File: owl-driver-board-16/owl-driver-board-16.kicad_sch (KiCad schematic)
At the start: 80 parts, among them J10 1890963, J11 ENABLE, J2 RASPBERRYPI-40-PIN-GPIO, J25 CONN_04X2, J27 CONN_04X2, J29 CONN_04X2, J6 CONN_04X2, J9 PI 5V, U1 TPS54531DDA, U3 LM73100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

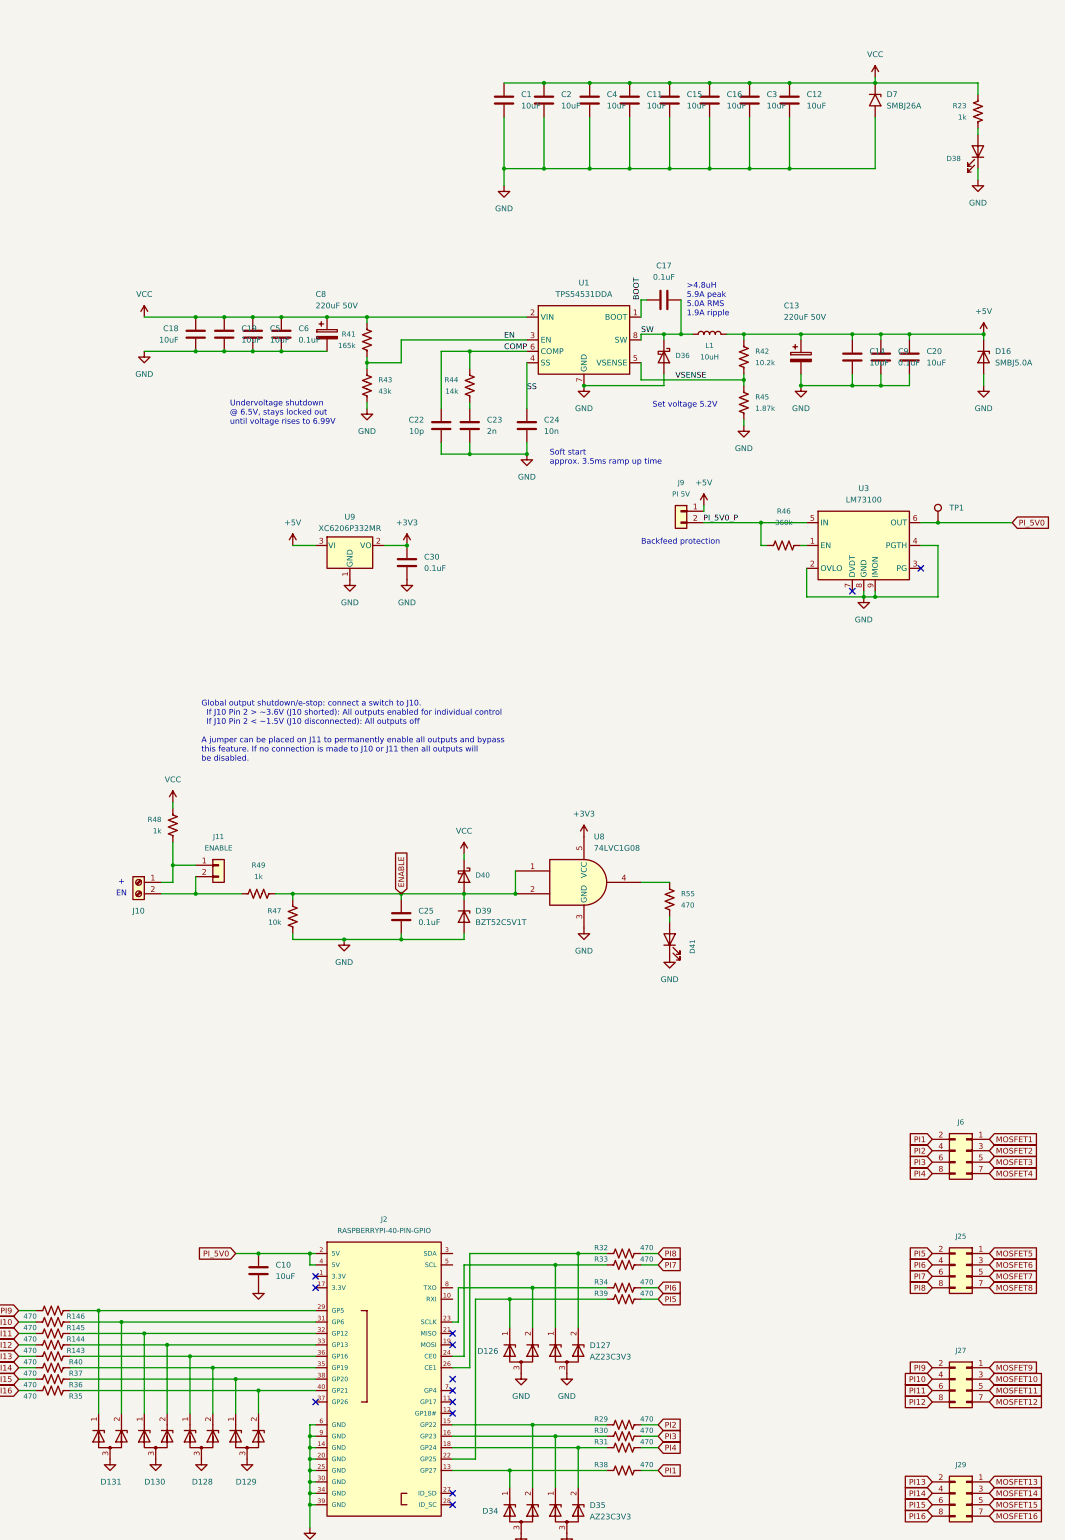
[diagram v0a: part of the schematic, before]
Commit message: add a 16-way version
Add a 16-way version of the HAT. Drop the PWM controller to focus on
GPIO control of 16 outputs, with output enable/e-stop, and keeping the
25W Pi power supply.

This version (v1.0) has a small bug in the panel, fixed in v1.1.
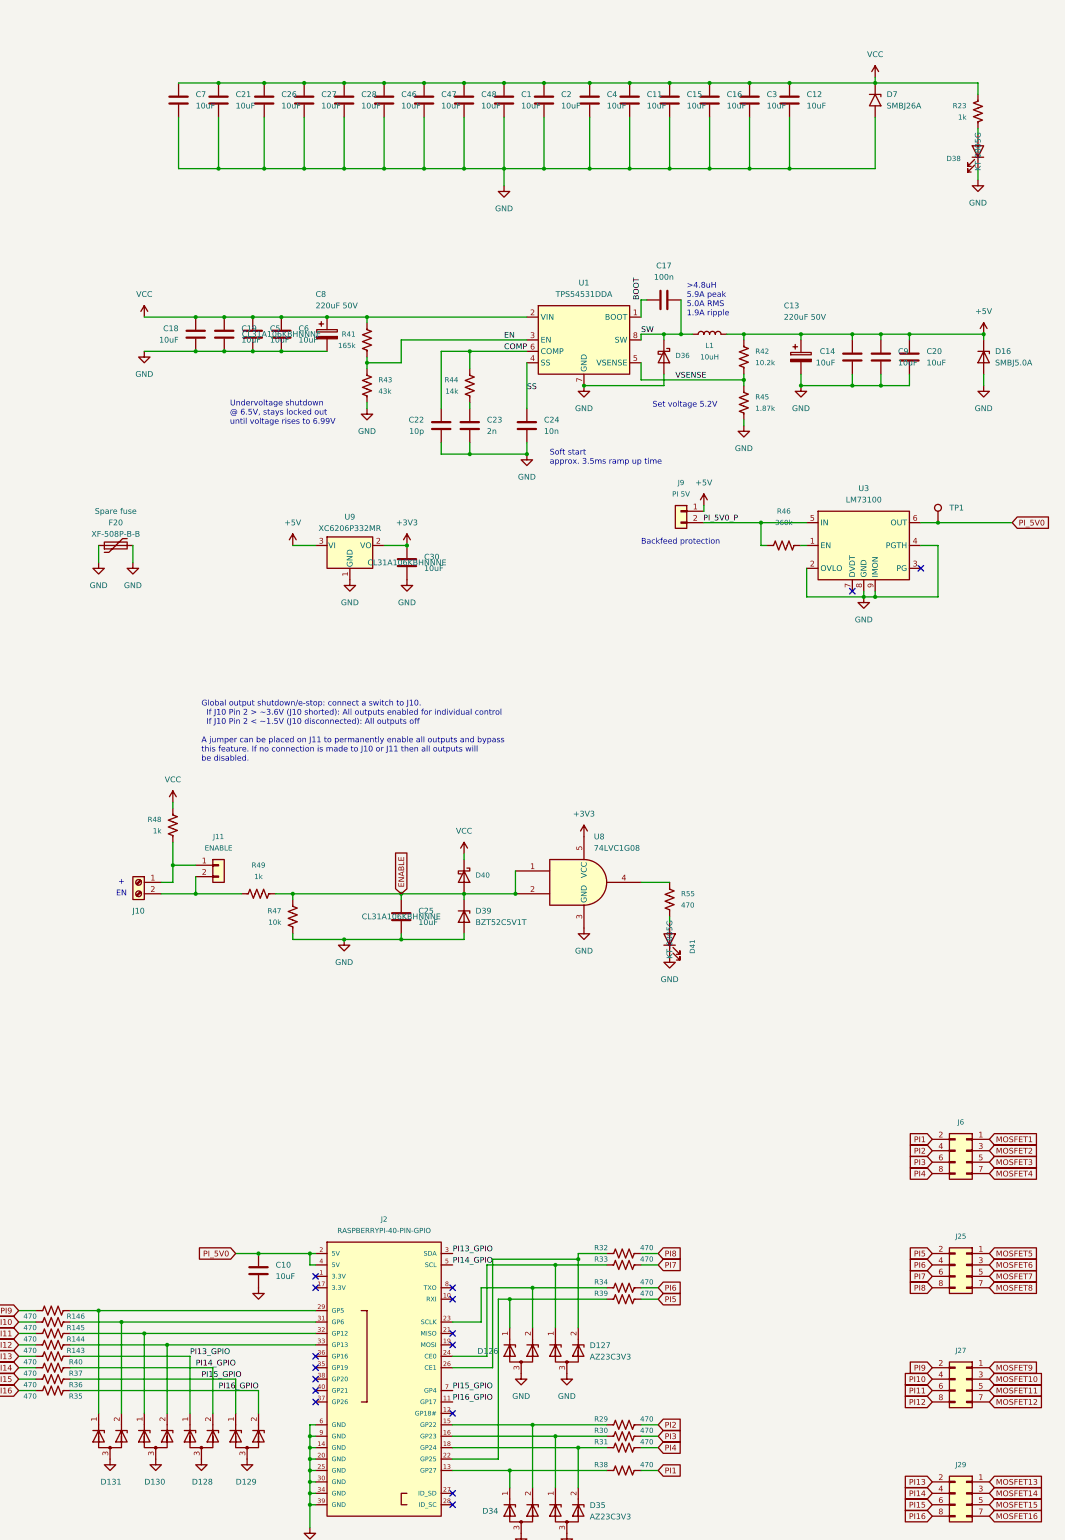
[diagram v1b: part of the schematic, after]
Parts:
- added C21, C26, C27, C28, C46, C47, C48, C7: 10uF, misc:C_1206_3216Metric_nosilk, symbol Device:C
- added F20: XF-508P-B-B, Fuse:Fuseholder_Blade_Mini_Keystone_3568, symbol Device:Polyfuse
- C1, C10, C11, C12, C14, C15, C16, C18, C19, C2, C20, C3, C4, C5: LCSC C89835 -> C13585; Part 1206X106K500CT -> CL31A106KBHNNNE
- C17: value 0.1uF -> 100n; footprint misc:C_0603_1608Metric_nosilk -> misc:C_0402_1005Metric_nosilk; LCSC C14663 -> C307331; Part (none) -> CL05B104KB54PNC
- C22: footprint Capacitor_SMD:C_0805_2012Metric -> misc:C_0603_1608Metric_nosilk; LCSC C107107 -> C1634; Part CC0805JRNPO9BN100 -> CL10C100JB8NNNC
- C24: LCSC C77053 -> C57112; Part GRM188R71H103KA01D -> 0603B103K500NT
- C25, C30, C6, C9: value 0.1uF -> 10uF; footprint misc:C_0603_1608Metric_nosilk -> misc:C_1206_3216Metric_nosilk; LCSC C14663 -> C13585; Part (none) -> CL31A106KBHNNNE
- D38, D41: value SZYY0805YG -> KT-0805G; LCSC C434435 -> C2297; Part (none) -> KT-0805G
- J25, J27, J29, J6: footprint Connector_PinHeader_2.54mm:PinHeader_2x04_P2.54mm_Vertical -> misc:Connector_PinHeader_2x04_P2.54mm_Vertical_nosilk
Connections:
- net GND: now also C21.2, C26.2, C27.2, C28.2, C46.2, C47.2, C48.2, C7.2, F20.1, F20.2
- net VCC: now also C21.1, C26.1, C27.1, C28.1, C46.1, C47.1, C48.1, C7.1
- net PI14_GPIO: now reaches D128.2 (K), R37.1
- net PI14_GPIO: now also J2.5 (SCL); no longer J2.35 (GP19)
- net PI15_GPIO: now reaches D129.1 (K), R36.1
- net PI15_GPIO: now also J2.7 (GP4); no longer J2.38 (GP20)
- net PI16_GPIO: now reaches D129.2 (K), R35.1
- net PI16_GPIO: now also J2.11 (GP17); no longer J2.40 (GP21)
- net PI13_GPIO: now reaches J2.3 (SDA)
- net PI13_GPIO: now also D128.1 (K), R40.1
- now unconnected: J2.36 (GP16)
- no-connect marks 13 -> 16
